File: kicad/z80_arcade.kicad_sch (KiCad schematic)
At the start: 1 part, among them U1 Z80B

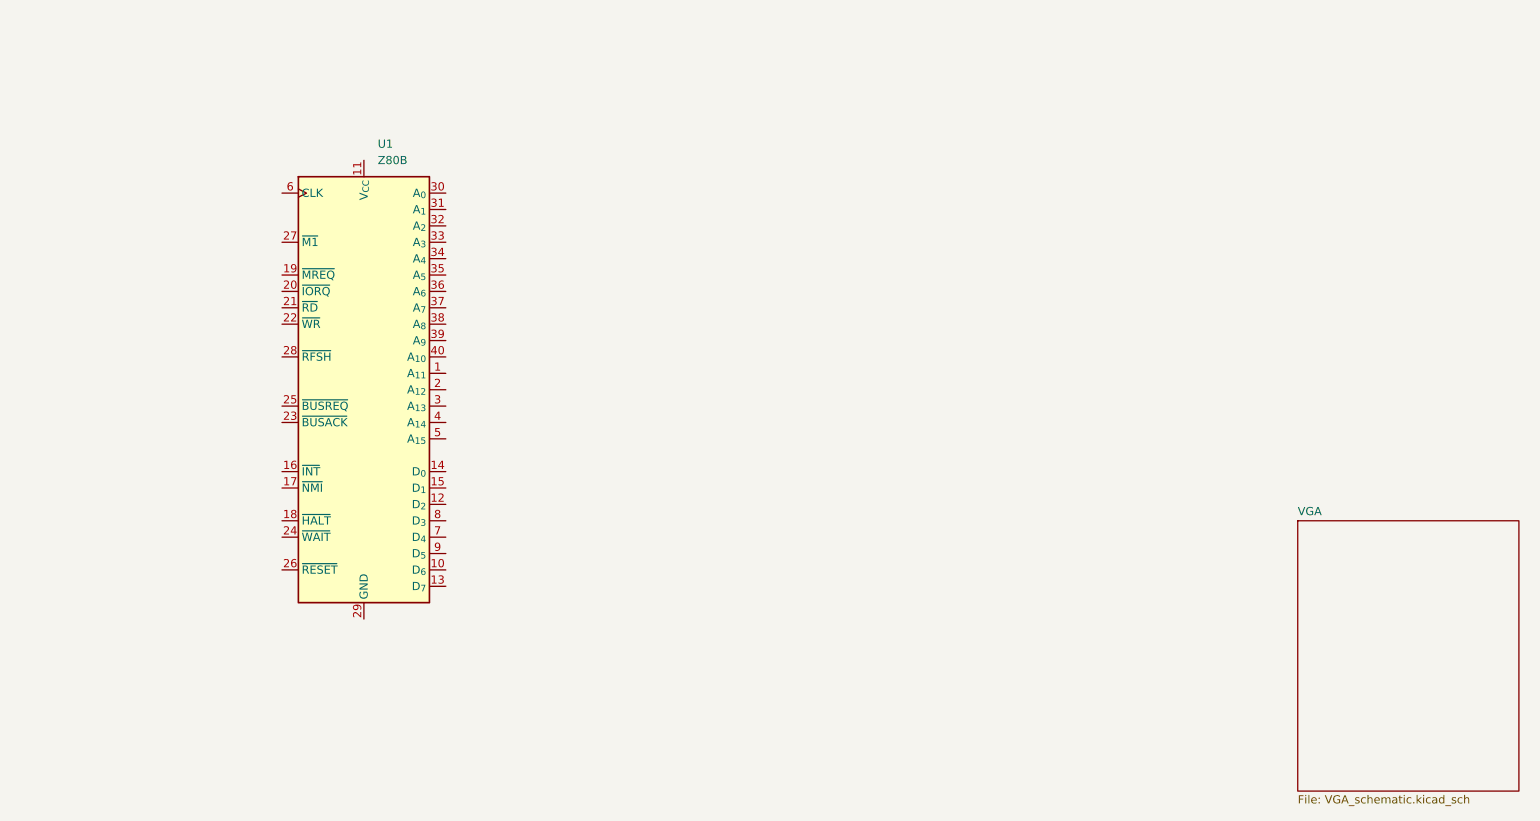
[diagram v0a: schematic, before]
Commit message: Add AT28C64 symbol. Tidy up HSYNC schematic. Add EEPROM - Z80 connection and VGA - Z80 connection
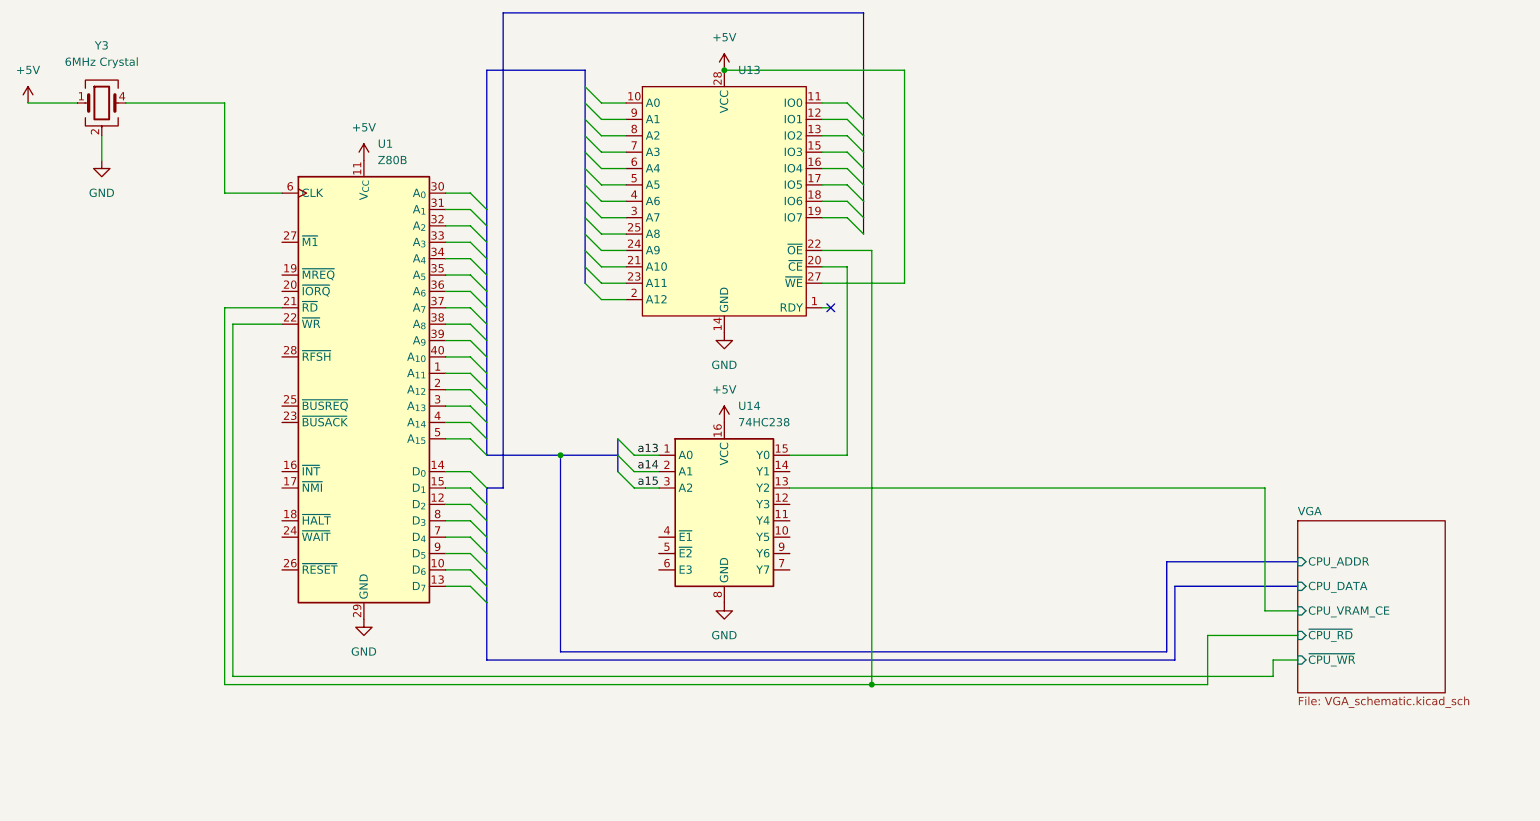
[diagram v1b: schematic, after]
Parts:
- added U13: (no value), symbol MyLibrary:AT28C64
- added U14: 74HC238, symbol 74xx:74HC238
- added Y3: 6MHz Crystal, symbol Device:Crystal_GND23
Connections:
- net +5V: now reaches U1.11 (V_{CC})
- net +5V: now also U13.27 (~{WE}), U13.28 (VCC), U14.16 (VCC), Y3.1
- net VGA/~{CPU_RD}: now reaches U1.21 (~{RD})
- net VGA/~{CPU_RD}: now also U13.22 (~{OE})
- net VGA/~{CPU_WR}: now reaches U1.22 (~{WR})
- net GND: now reaches U1.29 (GND)
- net GND: now also U13.14 (GND), U14.8 (GND), Y3.2 (G), Y3.3 (G)
- net at U1.6 (CLK): now also Y3.4
- new net: U13.20 (~{CE}), U14.15 (Y0)
- new net VGA/CPU_VRAM_CE: U14.13 (Y2)
- new net a13: U14.1 (A0)
- new net a14: U14.2 (A1)
- new net a15: U14.3 (A2)
- no-connect marks 0 -> 1
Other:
- sheet VGA ports: added CPU_ADDR, CPU_DATA, CPU_VRAM_CE, ~{CPU_RD}, ~{CPU_WR}; removed none
